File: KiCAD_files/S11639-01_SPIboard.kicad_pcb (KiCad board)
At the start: 4 copper layers, 70 x 40 mm, 60 parts, among them IC1 74LVC1T45GW,125, IC2 74LVC1T45GW,125, IC3 74LVC1T45GW,125, IC4 MCP33131D-10-I_MS, IC5 74LVC1T45GW,125, J1 Conn_01x03_Male, J2 Conn_02x10_Odd_Even, J3 705430001, J4 Conn_01x03_Male, U1 ADA4807-2ARMZ-R7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

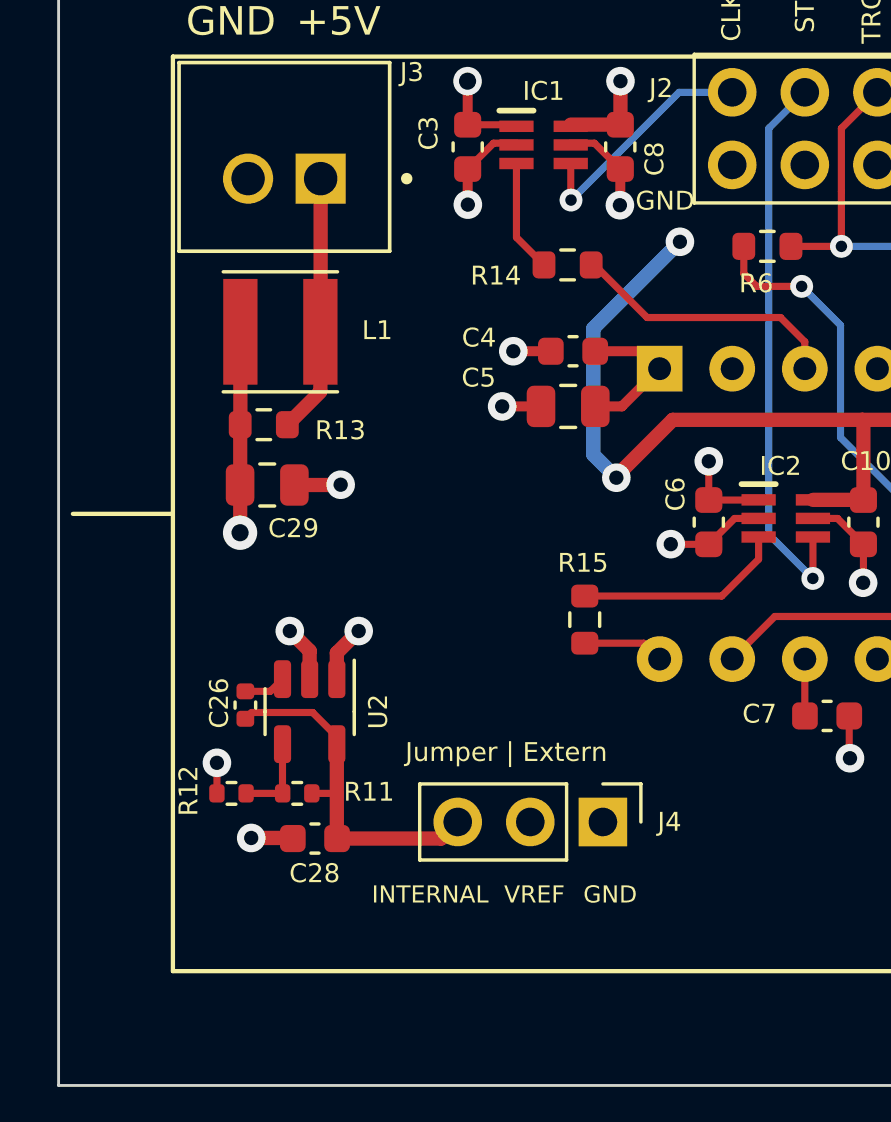
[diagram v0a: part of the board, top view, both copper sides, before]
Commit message: upgrade input power filter
Adds input side cap to the inductive input filter.
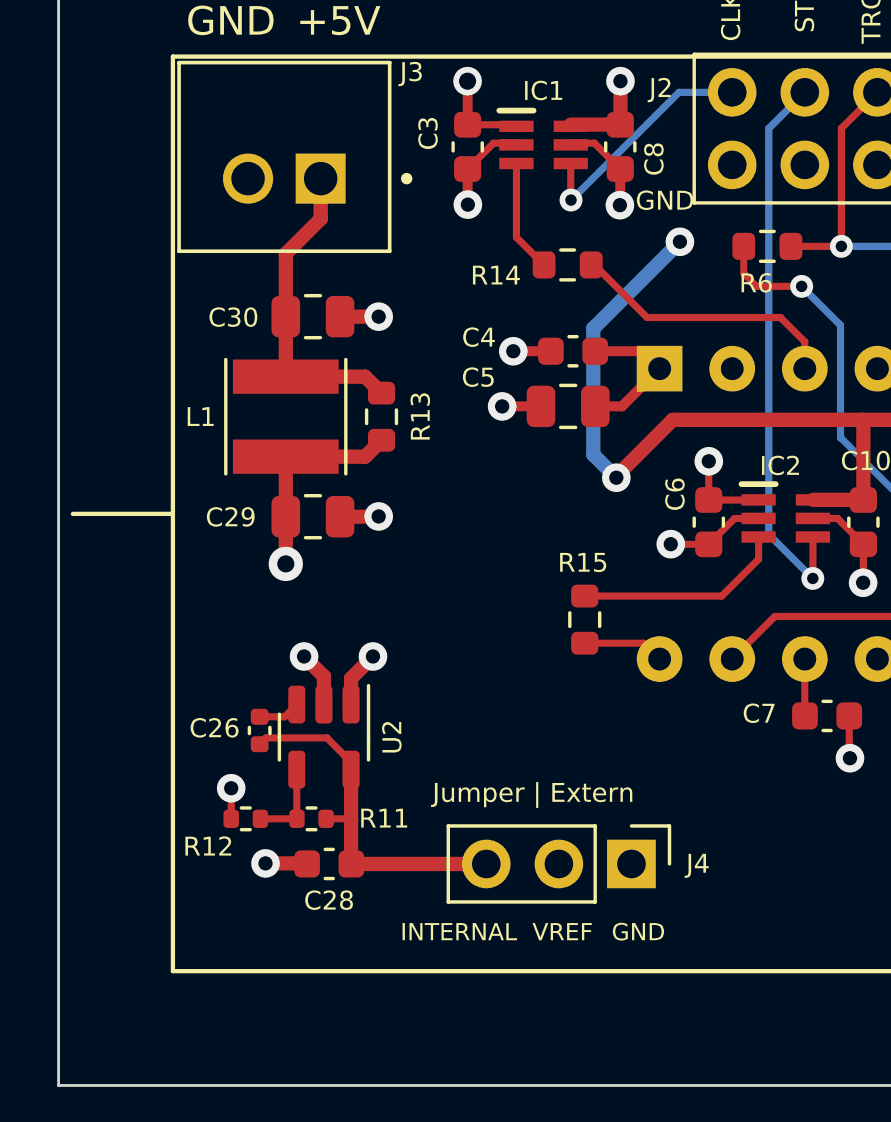
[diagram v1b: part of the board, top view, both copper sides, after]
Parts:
- added C30: 22uF, Capacitor_SMD:C_0805_2012Metric, F.Cu at (103.9, 93.1)
- moved R13 4.13 mm to (106.3, 96.6), turned to -90 degrees
- moved L1 2.98 mm to (103.0, 96.6), turned to -90 degrees
- moved C29 1.95 mm to (103.9, 100.1)
- moved J4 1.78 mm to (115.0, 112.2)
- moved C26 1.02 mm to (102.0, 107.6)
- moved C28 1.02 mm to (104.5, 112.2)
- moved R11 1.02 mm to (103.8, 110.7)
- moved R12 1.02 mm to (101.5, 110.7)
- moved U2 1.02 mm to (104.3, 107.8)
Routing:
- net /+4_6.5V_input: track 9.09 -> 11.0 mm
- net Earth: track 57.2 -> 58.3 mm, vias 30 -> 31
